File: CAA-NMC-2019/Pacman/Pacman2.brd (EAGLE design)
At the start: 40 x 40 mm, 10 parts, among them IC1 ATTINY85-20SU, J1 M20-9980346

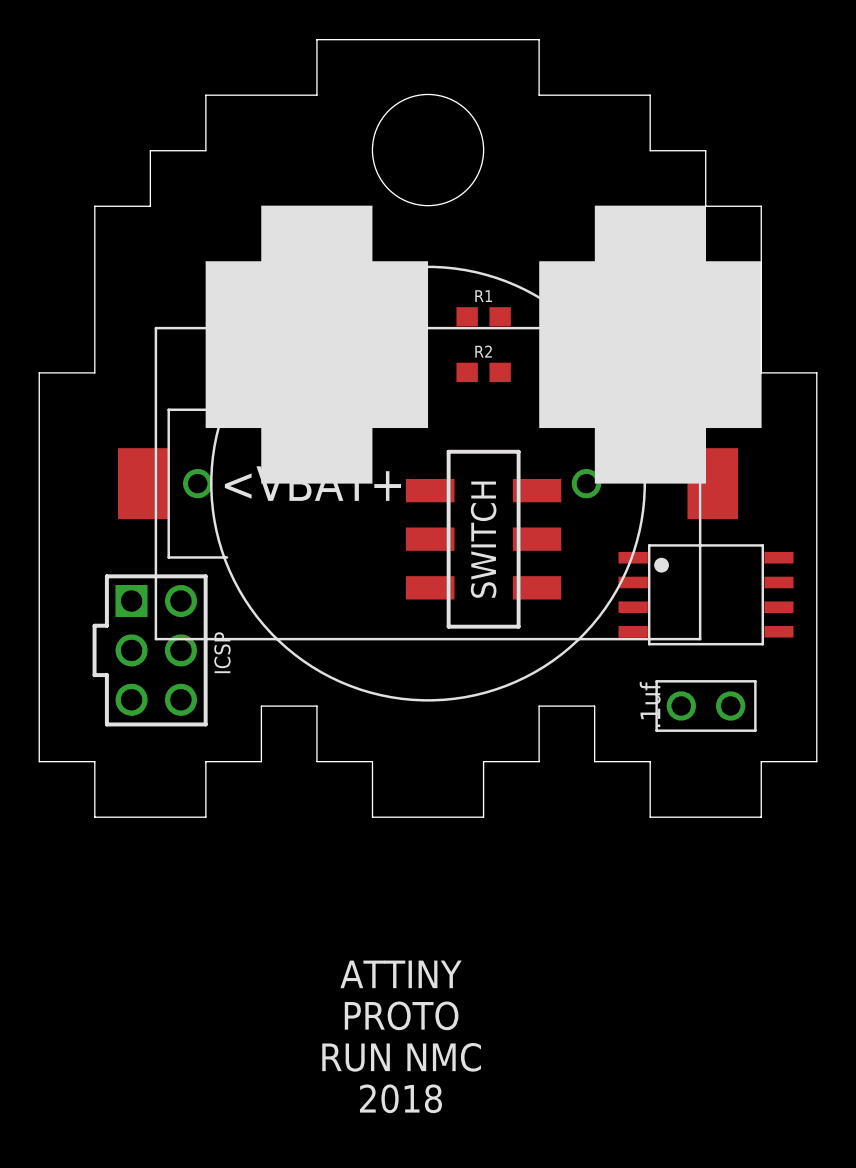
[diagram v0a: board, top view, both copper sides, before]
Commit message: added silk outline, mirrored battery parts
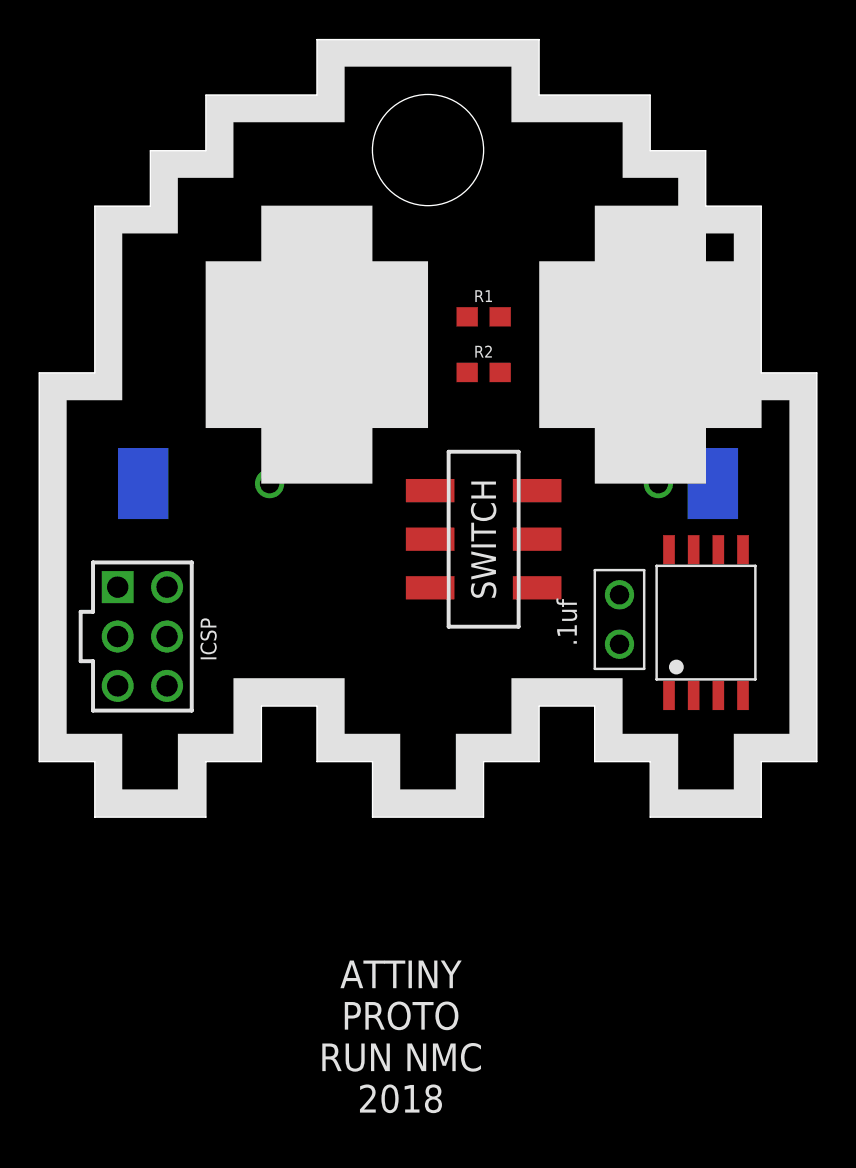
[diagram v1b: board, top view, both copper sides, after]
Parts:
- moved U$123 8.09 mm to (9.85, 11.4), turned to 270 degrees
- moved IC1 1.43 mm to (14.3, 10.0), turned to 90 degrees
- moved J1 1.01 mm to (-12.2, 9.29)
- flipped U$2 to the bottom
- flipped U$3 to the bottom

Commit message: visual improvements, replaced cap w/ surface mount
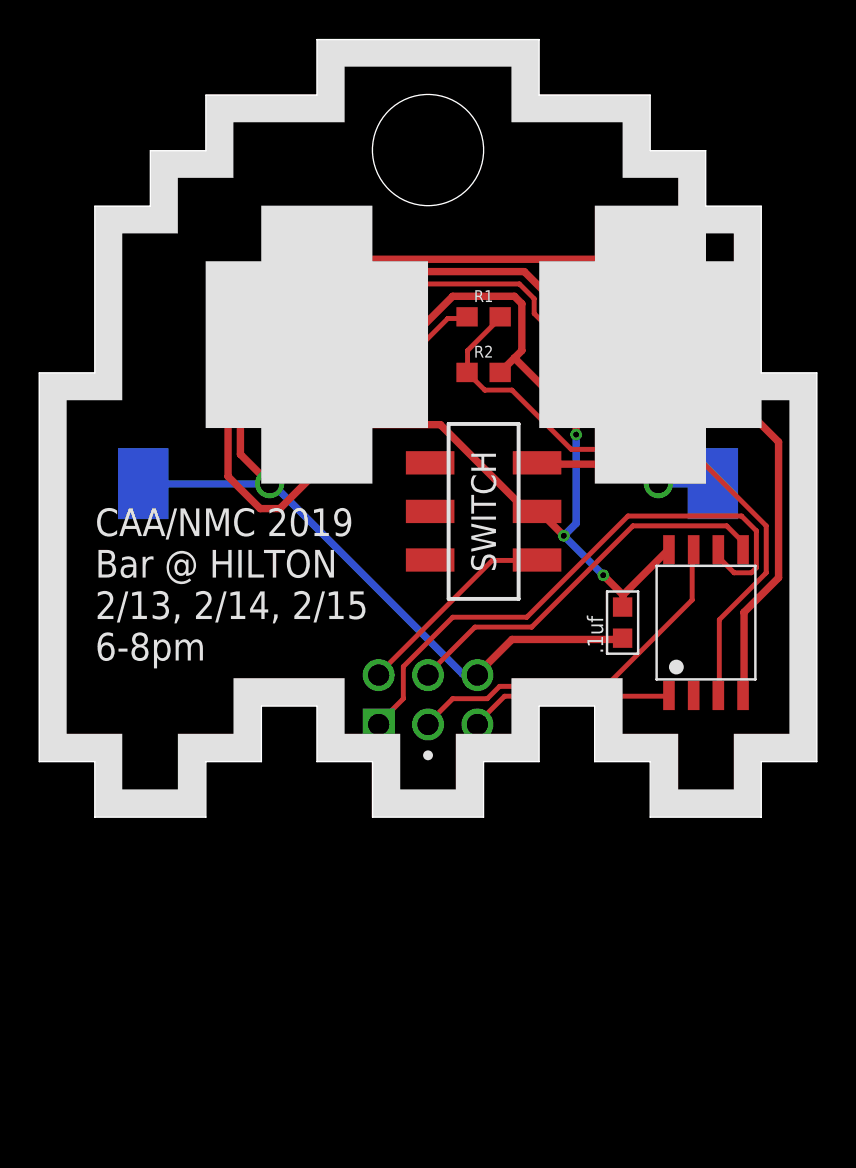
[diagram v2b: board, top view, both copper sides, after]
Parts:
- removed J1: M20-9980346, BadgeParts:HDRV6W64P254_2X3_762X508X868P
- removed U$123: DECOUPLING_CAP, BadgeParts:DECOUPLING_CAP
- added DECOUPLER: .1uf, BadgeParts:0603-CAP
- added J2: ICSP-LO-SILK, BadgeParts:ICSP-LO-SILK
- moved U$145 1.43 mm to (2.86, 15.7)
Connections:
- net GND: now also DECOUPLER.CAP1, J2.GND; no longer J1.GND, U$123.P$1
- net PB0: now also J2.0/MOSI/SDA; no longer J1.0/MOSI/SDA
- net PB1: now also J2.1/MISO; no longer J1.1/MISO
- net PB2: now also J2.2/SCK/SCL; no longer J1.2/SCK/SCL
- net PB5: now also J2.5/RST; no longer J1.5/RST
- net VCC: now also DECOUPLER.CAP2; no longer U$123.P$2
- net VUSB: now also J2.VCC; no longer J1.VCC
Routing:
- net VCC: track 0.00 -> 99.5 mm, vias 0 -> 3
- net GND: track 0.00 -> 86.0 mm
- net PB4: track 0.00 -> 31.9 mm
- net PB1: track 0.00 -> 29.9 mm
- net PB0: track 0.00 -> 20.2 mm
- net PB2: track 0.00 -> 18.9 mm
- net N$3: track 0.00 -> 17.0 mm
- net N$5: track 0.00 -> 12.2 mm
- net VUSB: track 0.00 -> 10.6 mm
- net PB5: track 0.00 -> 10.5 mm
- net VBAT: track 0.00 -> 9.51 mm
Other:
- board text added: "BIT.LY/BADGECULTURE"
- board text added: "BONTRAGER"
- board text added: "CAA/NMC 2019 Bar @ HILTON 2/13, 2/14, 2/15 6-8pm"
- board text added: "HOKANSON"
- board text removed: ".1uf"
- board text removed: "ATTINY PROTO RUN NMC 2018"
- board text removed: "HOKANSON/BONTRAGER BIT.LY/BADGECULTURE"

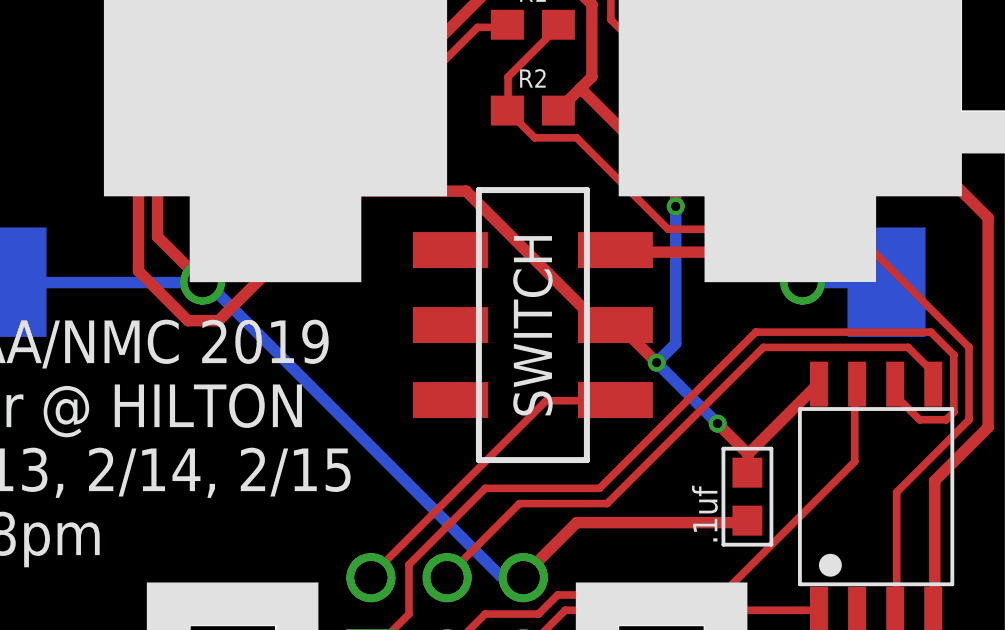
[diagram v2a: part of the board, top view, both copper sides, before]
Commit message: added OSH silk
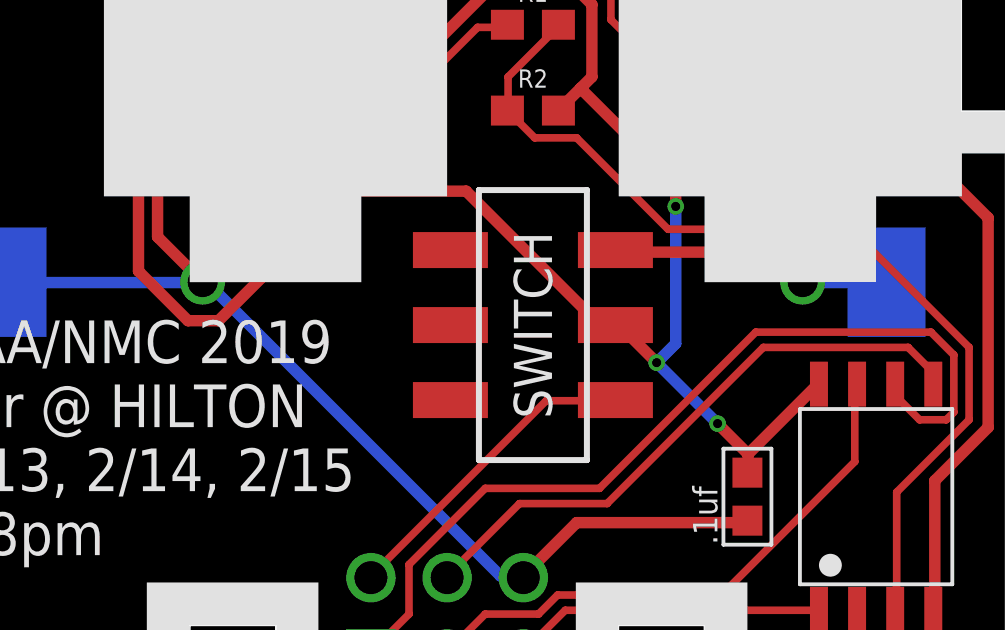
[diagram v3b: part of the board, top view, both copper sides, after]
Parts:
- added U$5: (no value), NickParts:OSHPARK_LOGOHEX
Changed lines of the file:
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@@
 </class>
 </classes>
-<designrules name="SeeedStudio_2layer_DRU_no_angle_20140221">
-<description language="de">&lt;b&gt;EAGLE Design Rules&lt;/b&gt;
+<designrules name="oshpark-2layer">
+<description language="en">&lt;b&gt;OSH Park Design Rules&lt;/b&gt;
 &lt;p&gt;
-Die Standard-Design-Rules sind so gewählt, dass sie für
-die meisten Anwendungen passen. Sollte ihre Platine
-besondere Anforderungen haben, treffen Sie die erforderlichen
-Einstellungen hier und speichern die Design Rules unter
-einem neuen Namen ab.</description>
-<description language="en">&lt;b&gt;EAGLE Design Rules&lt;/b&gt;
+Please make sure your boards conform to these design rules.
+&lt;/p&gt;
 &lt;p&gt;
-The default Design Rules have been set to cover
-a wide range of applications. Your particular design
-may have different requirements, so please make the
-necessary adjustments and save your customized
-design rules under a new name.</description>
-<description language="zh">&lt;b&gt;Seeed Studio EAGLE Design Rules&lt;/b&gt;
-</description>
+Note, that not all DRC settings must be set by the manufacturer. Several can be adjusted for the design, including those listed on our docs page here.
+&lt;a href=&quot;http://docs.oshpark.com/design-tools/eagle/design-rules-files/&quot;&gt;Adjustable Settings&lt;/a&gt;
+&lt;/p&gt;</description>
 <param name="layerSetup" value="(1*16)"/>
-<param name="mtCopper" value="0.035mm 0.0175mm 0.035mm 0.035mm 0.035mm 0.035mm 0.035mm 0.035mm 0.035mm 0.035mm 0.035mm 0.035mm 0.035mm 0.035mm 0.0175mm 0.035mm"/>
-<param name="mtIsolate" value="1.5mm 1.1mm 0.2mm 0.15mm 0.2mm 0.15mm 0.2mm 0.15mm 0.2mm 0.15mm 0.2mm 0.15mm 0.2mm 0.15mm 0.2mm"/>
+<param name="mtCopper" value="0.035559375mm 0.0356mm 0.0356mm 0.0356mm 0.0356mm 0.0356mm 0.0356mm 0.0356mm 0.0356mm 0.0356mm 0.0356mm 0.0356mm 0.0356mm 0.0356mm 0.0356mm 0.035559375mm"/>
+<param name="mtIsolate" value="1.6mm 0.1499mm 0.2007mm 0.1499mm 0.2007mm 0.1499mm 0.2007mm 0.1499mm 0.2007mm 0.1499mm 0.2007mm 0.1499mm 0.2007mm 0.1499mm 0.2007mm"/>
 <param name="mdWireWire" value="6mil"/>
 <param name="mdWirePad" value="6mil"/>
@@
 <param name="mdPadVia" value="6mil"/>
 <param name="mdViaVia" value="6mil"/>
-<param name="mdSmdPad" value="0mil"/>
-<param name="mdSmdVia" value="0mil"/>
-<param name="mdSmdSmd" value="0mil"/>
+<param name="mdSmdPad" value="6mil"/>
+<param name="mdSmdVia" value="6mil"/>
+<param name="mdSmdSmd" value="6mil"/>
 <param name="mdViaViaSameLayer" value="8mil"/>
 <param name="mnLayersViaInSmd" value="2"/>
-<param name="mdCopperDimension" value="10mil"/>
-<param name="mdDrill" value="10mil"/>
+<param name="mdCopperDimension" value="15mil"/>
+<param name="mdDrill" value="6mil"/>
 <param name="mdSmdStop" value="0mil"/>
 <param name="msWidth" value="6mil"/>
-<param name="msDrill" value="12mil"/>
-<param name="msMicroVia" value="12mil"/>
+<param name="msDrill" value="10mil"/>
+<param name="msMicroVia" value="10mil"/>
 <param name="msBlindViaRatio" value="0.5"/>
 <param name="rvPadTop" value="0.25"/>
@@
 <param name="rvMicroViaOuter" value="0.25"/>
 <param name="rvMicroViaInner" value="0.25"/>
-<param name="rlMinPadTop" value="10mil"/>
+<param name="rlMinPadTop" value="5mil"/>
 <param name="rlMaxPadTop" value="20mil"/>
-<param name="rlMinPadInner" value="10mil"/>
+<param name="rlMinPadInner" value="5mil"/>
 <param name="rlMaxPadInner" value="20mil"/>
-<param name="rlMinPadBottom" value="10mil"/>
+<param name="rlMinPadBottom" value="5mil"/>
 <param name="rlMaxPadBottom" value="20mil"/>
-<param name="rlMinViaOuter" value="6mil"/>
+<param name="rlMinViaOuter" value="5mil"/>
 <param name="rlMaxViaOuter" value="20mil"/>
-<param name="rlMinViaInner" value="6mil"/>
+<param name="rlMinViaInner" value="5mil"/>
 <param name="rlMaxViaInner" value="20mil"/>
-<param name="rlMinMicroViaOuter" value="4mil"/>
+<param name="rlMinMicroViaOuter" value="5mil"/>
 <param name="rlMaxMicroViaOuter" value="20mil"/>
-<param name="rlMinMicroViaInner" value="4mil"/>
+<param name="rlMinMicroViaInner" value="5mil"/>
 <param name="rlMaxMicroViaInner" value="20mil"/>
 <param name="psTop" value="-1"/>
 <param name="psBottom" value="-1"/>
-<param name="psFirst" value="0"/>
+<param name="psFirst" value="-1"/>
 <param name="psElongationLong" value="100"/>
 <param name="psElongationOffset" value="100"/>
 <param name="mvStopFrame" value="1"/>
 <param name="mvCreamFrame" value="0"/>
-<param name="mlMinStopFrame" value="2mil"/>
-<param name="mlMaxStopFrame" value="2mil"/>
+<param name="mlMinStopFrame" value="2.5mil"/>
+<param name="mlMaxStopFrame" value="2.5mil"/>
 <param name="mlMinCreamFrame" value="0mil"/>
 <param name="mlMaxCreamFrame" value="0mil"/>
-<param name="mlViaStopLimit" value="100mil"/>
+<param name="mlViaStopLimit" value="0mil"/>
 <param name="srRoundness" value="0"/>
 <param name="srMinRoundness" value="0mil"/>
@@
 <param name="checkAngle" value="0"/>
 <param name="checkFont" value="1"/>
-<param name="checkRestrict" value="0"/>
+<param name="checkRestrict" value="1"/>
 <param name="checkStop" value="0"/>
 <param name="checkValues" value="0"/>
@@
 </element>
 <element name="J2" library="BadgeParts" package="ICSP-LO-SILK" value="ICSP-LO-SILK" x="0" y="8.58" smashed="yes" rot="R180"/>
+<element name="U$5" library="NickParts" library_urn="urn:adsk.eagle:library:4753178" package="OSHPARK_LOGOHEX" package3d_urn="urn:adsk.eagle:package:4912571/1" value="" x="-9.744" y="2.982" smashed="yes" rot="MR0"/>
 </elements>
 <signals>
